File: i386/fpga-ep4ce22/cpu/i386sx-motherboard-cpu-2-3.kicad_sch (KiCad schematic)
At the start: 1 part, among them U1 (2/3) NG80386SX-20

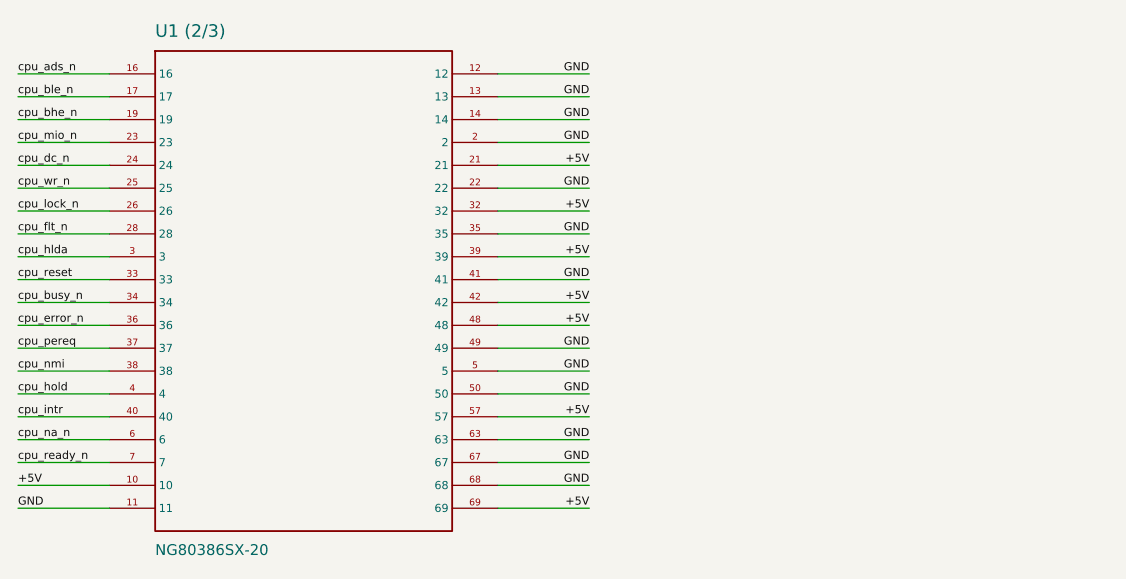
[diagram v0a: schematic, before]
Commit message: Publish the motherboards' KiCad files
From socket3@c0f6464 socket7@9205469 socket370@524f5b1 i386@bea926c
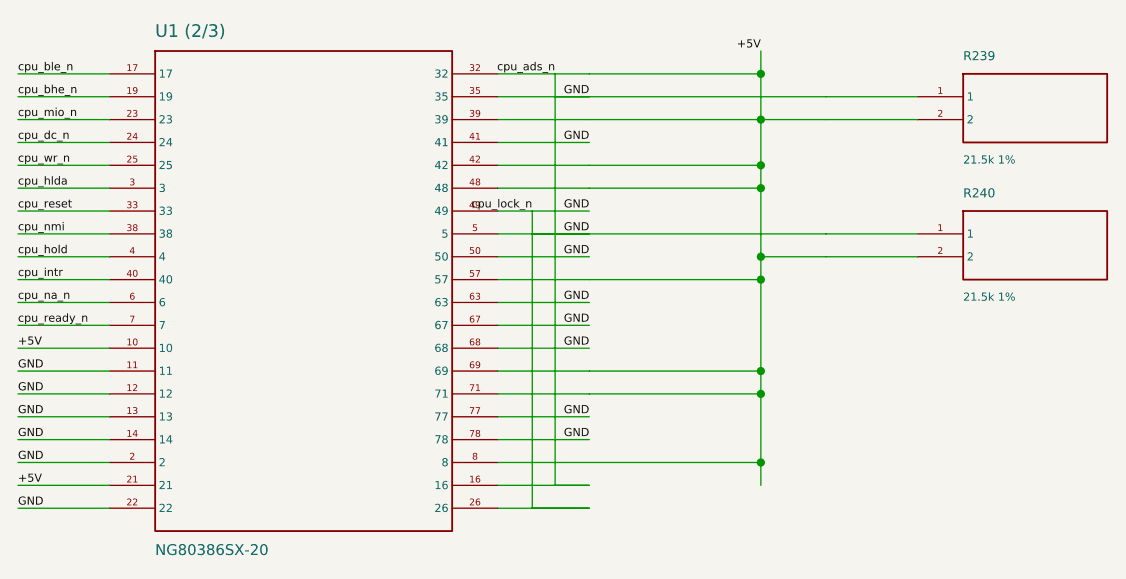
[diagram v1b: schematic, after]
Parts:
- added R239, R240: 21.5k 1%, symbol gen:S2_0s
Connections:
- net GND is gone; now on net +5V: U1 (2/3).11, U1 (2/3).12, U1 (2/3).13, U1 (2/3).14, U1 (2/3).2, U1 (2/3).22, U1 (2/3).35, U1 (2/3).41, U1 (2/3).49, U1 (2/3).5, U1 (2/3).50, U1 (2/3).63, U1 (2/3).67, U1 (2/3).68
- net cpu_ads_n is gone; now on net +5V: U1 (2/3).16
- net cpu_lock_n is gone; now on net +5V: U1 (2/3).26
- net +5V: now also U1 (2/3).71, U1 (2/3).77, U1 (2/3).78, U1 (2/3).8, R239.1, R239.2, R240.1, R240.2
- removed net cpu_busy_n: U1 (2/3).34
- removed net cpu_error_n: U1 (2/3).36
- removed net cpu_flt_n: U1 (2/3).28
- removed net cpu_pereq: U1 (2/3).37
